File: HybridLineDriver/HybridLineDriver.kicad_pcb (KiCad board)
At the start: 2 copper layers, 100 x 100 mm, 34 parts, among them J1 XLR3, J2 Conn_01x03, J3 Conn_01x02, U1 OPA1679

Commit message: update layout
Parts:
- moved R8 4.05 mm to (99.5, 100.5)
- moved R5 3.25 mm to (102.5, 105.0)
- moved R3 2.50 mm to (104.1, 92.5)
- moved R2 2.24 mm to (104.1, 95.5)
- moved R7 1.12 mm to (88.0, 90.0)
- moved R16 1.00 mm to (85.7, 95.5)
- moved C3 0.93 mm to (90.1, 98.0)
- moved R4 0.62 mm to (91.5, 101.5)
- moved C10 0.27 mm to (96.5, 105.9)
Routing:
- net Net-(C1-Pad2): track 30.2 -> 26.4 mm
- net Net-(U1C-+): track 15.0 -> 11.5 mm
- net Net-(U1C--): track 23.3 -> 21.1 mm
- net Net-(C6-Pad1): track 142.2 -> 140.6 mm
- net Net-(R2-Pad1): track 28.9 -> 27.7 mm
- net Net-(U1B--): track 17.1 -> 16.0 mm
- net Net-(C2-Pad1): track 94.6 -> 93.6 mm
- net Net-(R16-Pad2): track 15.7 -> 16.7 mm
- net Net-(U1D--): track 14.3 -> 13.3 mm
- net Net-(R7-Pad1): track 11.0 -> 11.8 mm
- net Net-(C3-Pad1): track 47.3 -> 46.7 mm
- net Net-(U1A--): track 9.80 -> 10.4 mm

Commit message: update layout
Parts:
- moved RV1 10.1 mm to (84.1, 83.2)
- moved C6 4.95 mm to (78.4, 133.6)
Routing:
- net Net-(C6-Pad1): track 140.6 -> 131.6 mm
- net Net-(C6-Pad2): track 9.82 -> 14.4 mm
- net Net-(R16-Pad2): track 16.7 -> 12.4 mm
- net Net-(R7-Pad1): track 11.8 -> 7.90 mm
- net GND: track 111.5 -> 110.0 mm
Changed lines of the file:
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@@
 	(footprint "Connector_PinHeader_2.54mm:PinHeader_1x03_P2.54mm_Vertical"
 		(layer "F.Cu")
-		(at 74 83 90)
+		(at 84.074 83.185 90)
 		(descr "Through hole straight pin header, 1x03, 2.54mm pitch, single row")
 		(tags "Through hole pin header THT 1x03 2.54mm single row")
@@
 	(footprint "Capacitor_THT:CP_Radial_D8.0mm_P3.50mm"
 		(layer "F.Cu")
-		(at 73.406 133.604 180)
+		(at 78.359 133.604 180)
 		(descr "CP, Radial series, Radial, pin pitch=3.50mm, , diameter=8mm, Electrolytic Capacitor")
 		(tags "CP Radial series Radial pin pitch 3.50mm  diameter 8mm Electrolytic Capacitor")
@@
 	)
 	(segment
-		(start 73.406 109.594)
-		(end 85.598 97.402)
+		(start 89 90)
+		(end 89.4625 90)
 		(width 0.254)
 		(layer "F.Cu")
@@
 	)
 	(segment
-		(start 104 104.9625)
-		(end 103.9625 105)
+		(start 117.799 128.41444)
+		(end 104.22744 141.986)
 		(width 0.254)
 		(layer "F.Cu")
@@
 	)
 	(segment
-		(start 85.598 97.402)
-		(end 85.598 93.402)
+		(start 85.598 93.402)
+		(end 89 90)
 		(width 0.254)
 		(layer "F.Cu")
@@
 	)
 	(segment
-		(start 75.184 141.986)
-		(end 73.406 140.208)
+		(start 104 104.9625)
+		(end 103.9625 105)
 		(width 0.254)
 		(layer "F.Cu")
@@
 	)
 	(segment
-		(start 117.799 124.437879)
-		(end 117.799 128.41444)
+		(start 78.359 104.641)
+		(end 85.598 97.402)
 		(width 0.254)
 		(layer "F.Cu")
@@
 	)
 	(segment
-		(start 117.799 128.41444)
-		(end 104.22744 141.986)
+		(start 85.598 97.402)
+		(end 85.598 93.402)
 		(width 0.254)
 		(layer "F.Cu")
@@
 	)
 	(segment
-		(start 73.406 133.604)
-		(end 73.406 109.594)
-		(width 0.254)
-		(layer "F.Cu")
-		(net 11)
-	)
-	(segment
-		(start 73.406 140.208)
-		(end 73.406 133.604)
+		(start 117.799 124.437879)
+		(end 117.7375 124.437879)
 		(width 0.254)
 		(layer "F.Cu")
@@
 	)
 	(segment
-		(start 117.799 124.437879)
-		(end 117.7375 124.437879)
+		(start 78.359 136.747)
+		(end 83.598 141.986)
 		(width 0.254)
 		(layer "F.Cu")
@@
 	)
 	(segment
-		(start 89 90)
-		(end 89.4625 90)
+		(start 104 91.5)
+		(end 104 104.9625)
 		(width 0.254)
 		(layer "F.Cu")
@@
 	)
 	(segment
-		(start 104.22744 141.986)
-		(end 75.184 141.986)
+		(start 117.799 124.437879)
+		(end 117.799 128.41444)
 		(width 0.254)
 		(layer "F.Cu")
@@
 	)
 	(segment
-		(start 104 91.5)
-		(end 104 104.9625)
+		(start 78.359 133.604)
+		(end 78.359 136.747)
 		(width 0.254)
 		(layer "F.Cu")
@@
 	)
 	(segment
-		(start 85.598 93.402)
-		(end 89 90)
+		(start 83.598 141.986)
+		(end 104.22744 141.986)
 		(width 0.254)
 		(layer "F.Cu")
@@
 	)
 	(segment
-		(start 69.906 133.604)
-		(end 64.516 133.604)
+		(start 78.359 133.604)
+		(end 78.359 104.641)
 		(width 0.254)
 		(layer "F.Cu")
-		(net 12)
+		(net 11)
 	)
 	(segment
@@
 	)
 	(segment
-		(start 69.906 133.604)
-		(end 69.652 133.858)
+		(start 60.706 133.843)
+		(end 60.706 133.604)
 		(width 0.254)
 		(layer "F.Cu")
@@
 	)
 	(segment
-		(start 60.706 133.843)
-		(end 60.706 133.604)
+		(start 74.859 133.604)
+		(end 64.516 133.604)
 		(width 0.254)
 		(layer "F.Cu")
@@
 	)
 	(segment
-		(start 81.04 87.5)
-		(end 76.54 83)
-		(width 0.254)
-		(layer "F.Cu")
-		(net 15)
-	)
-	(segment
 		(start 64.516 130.679)
 		(end 64.516 122.174)
@@
 	)
 	(segment
-		(start 83.5 87.5)
-		(end 81.04 87.5)
-		(width 0.254)
-		(layer "F.Cu")
-		(net 15)
-	)
-	(segment
 		(start 108.799621 143.168379)
 		(end 128.016 123.952)
@@
 	)
 	(segment
+		(start 76.708 140.5235)
+		(end 76.708 133.096)
+		(width 0.254)
+		(layer "F.Cu")
+		(net 15)
+	)
+	(segment
 		(start 97.731379 121.353379)
 		(end 97.79 121.412)
@@
 	)
 	(segment
+		(start 70.612 127)
+		(end 70.612 122.174)
+		(width 0.254)
+		(layer "F.Cu")
+		(net 15)
+	)
+	(segment
 		(start 94.488 103.378)
 		(end 94.488 103.632)
@@
 	)
 	(segment
+		(start 85.725 87.63)
+		(end 86.614 86.741)
+		(width 0.254)
+		(layer "F.Cu")
+		(net 15)
+	)
+	(segment
 		(start 87.827 124.437879)
 		(end 83.842121 124.437879)
@@
 	)
 	(segment
+		(start 86.614 86.741)
+		(end 86.614 83.185)
+		(width 0.254)
+		(layer "F.Cu")
+		(net 15)
+	)
+	(segment
 		(start 112.7145 123.19)
 		(end 114.3 123.19)
@@
 	)
 	(segment
-		(start 99.003 143.168379)
-		(end 108.799621 143.168379)
+		(start 76.708 133.096)
+		(end 70.612 127)
 		(width 0.254)
 		(layer "F.Cu")
@@
 	)
 	(segment
-		(start 96.5 100.5)
-		(end 98.0375 100.5)
+		(start 99.003 143.168379)
+		(end 108.799621 143.168379)
 		(width 0.254)
 		(layer "F.Cu")
@@
 	)
 	(segment
-		(start 76.708 140.5235)
-		(end 76.708 122.174)
+		(start 96.5 100.5)
+		(end 98.0375 100.5)
 		(width 0.254)
 		(layer "F.Cu")
@@
 	)
 	(via
-		(at 83.5 87.5)
+		(at 85.725 87.63)
 		(size 0.8)
 		(drill 0.4)
@@
 	)
 	(via
-		(at 76.708 122.174)
+		(at 70.612 122.174)
 		(size 0.8)
 		(drill 0.4)
@@
 	)
 	(segment
-		(start 79.08 83)
-		(end 82.0375 83)
+		(start 89.154 86.741)
+		(end 86.5375 89.3575)
 		(width 0.254)
 		(layer "F.Cu")
@@
 	)
 	(segment
-		(start 82.0375 83)
-		(end 86.5375 87.5)
+		(start 86.5375 89.3575)
+		(end 86.5375 90)
 		(width 0.254)
 		(layer "F.Cu")
@@
 	)
 	(segment
-		(start 86.5375 87.5)
-		(end 86.5375 90)
+		(start 89.154 83.185)
+		(end 89.154 86.741)
 		(width 0.254)
 		(layer "F.Cu")
@@
 	)
 	(segment
+		(start 84.201 93.193)
+		(end 84.201 83.312)
+		(width 0.254)
+		(layer "F.Cu")
+		(net 21)
+	)
+	(segment
+		(start 84.201 83.312)
+		(end 84.074 83.185)
+		(width 0.254)
+		(layer "F.Cu")
+		(net 21)
+	)
+	(segment
 		(start 84.197 95.5)
 		(end 84.197 93.197)
@@
 	(segment
 		(start 84.197 93.197)
-		(end 74 83)
+		(end 84.201 93.193)
 		(width 0.254)
 		(layer "F.Cu")

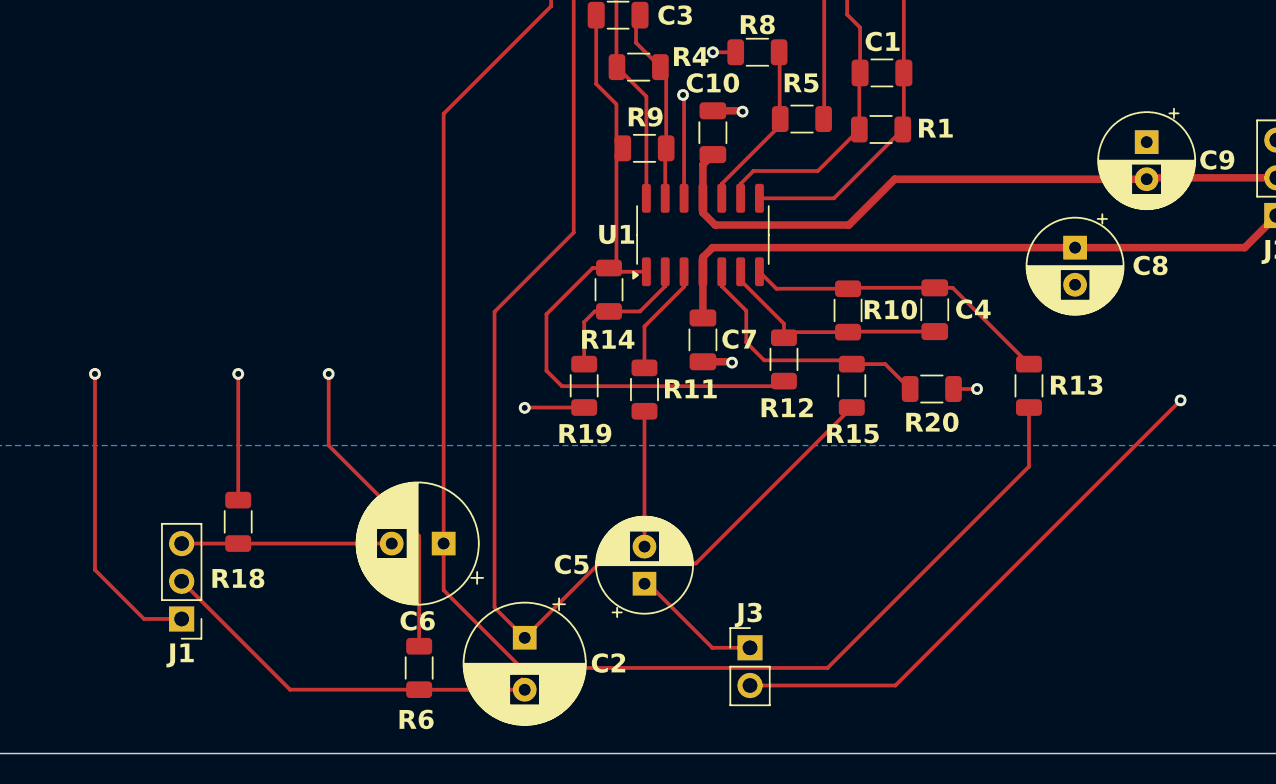
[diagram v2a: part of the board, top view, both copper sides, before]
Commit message: Update HybridLineDriver.kicad_pcb
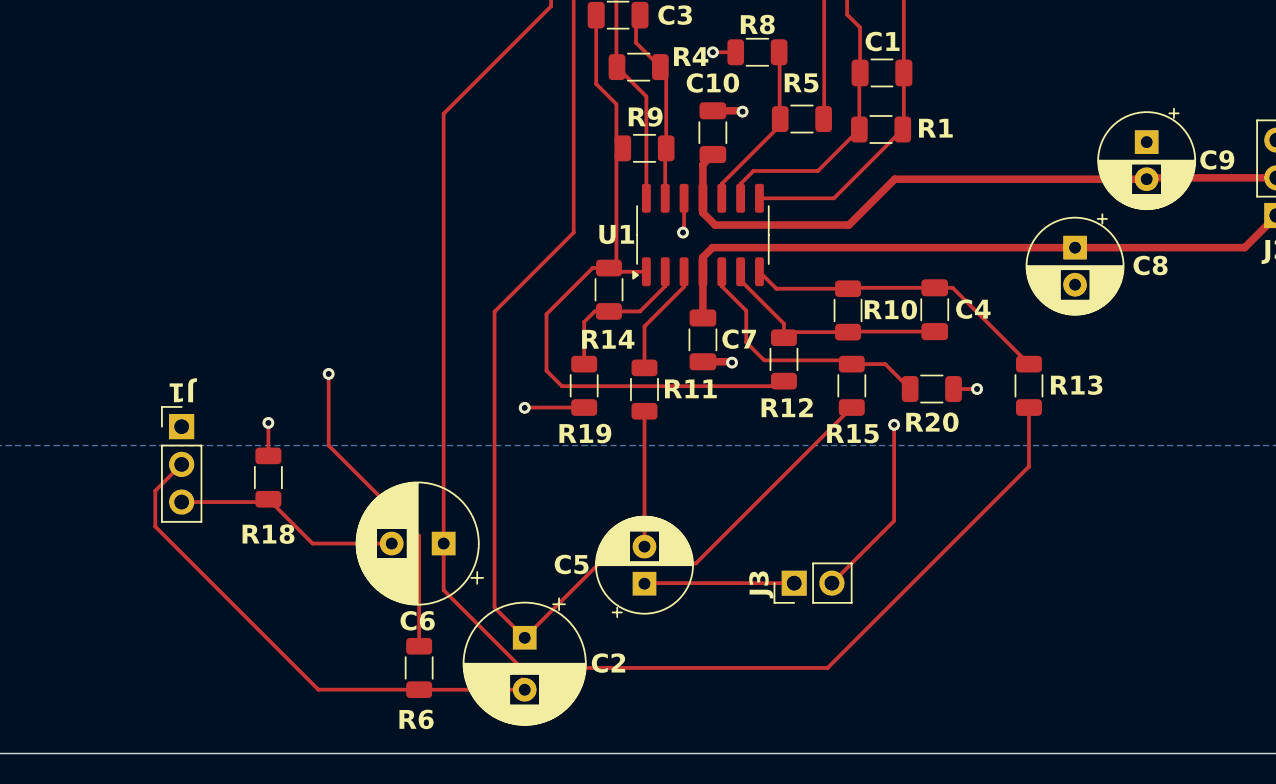
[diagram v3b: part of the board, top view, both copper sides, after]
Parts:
- moved J1 13.0 mm to (60.7, 125.7), turned to 0 degrees
- moved J3 5.28 mm to (102.0, 136.3), turned to 90 degrees
- moved R18 3.61 mm to (66.5, 129.2)
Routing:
- net GND: track 110.0 -> 53.8 mm, vias 11 -> 10
- net Net-(C2-Pad2): track 27.3 -> 35.2 mm
- net Net-(J3-Pin_1): track 8.90 -> 10.1 mm
- net Net-(C6-Pad2): track 14.4 -> 15.5 mm

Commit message: massive pcb rework
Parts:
- moved J1 78.1 mm to (134.5, 100.2), turned to 180 degrees
- moved R18 70.9 mm to (128.5, 94.7), turned to 90 degrees
- moved R6 63.7 mm to (124.8, 100.2)
- moved C6 51.5 mm to (110.4, 93.2), turned to 0 degrees
- moved C2 50.3 mm to (116.2, 101.5), turned to 0 degrees
- moved J3 36.1 mm to (134.2, 120.1), turned to 0 degrees
- moved R13 35.6 mm to (86.2, 106.4), turned to 90 degrees
- moved R20 27.9 mm to (95.1, 100.4), turned to -90 degrees
- moved C3 27.0 mm to (100.7, 122.8)
- moved R15 26.1 mm to (92.8, 100.4), turned to 90 degrees
- moved C5 25.2 mm to (111.9, 120.9), turned to 180 degrees
- moved C4 24.6 mm to (90.6, 104.8), turned to 180 degrees
- moved R10 18.3 mm to (90.6, 107.4), turned to 180 degrees
- moved R4 18.3 mm to (102.0, 116.5), turned to 90 degrees
- moved RV1 17.3 mm to (97.5, 94.1)
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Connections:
- C3 pad 2: Net-(U1D--) -> Net-(U1B--)
- C4 pad 1: Net-(U1B--) -> Net-(U1D--)
- R10 pad 1: Net-(U1B--) -> Net-(U1D--)
- R12 pad 2: Net-(U1B--) -> Net-(U1D--)
- R15 pad 1: Net-(U1B-+) -> Net-(U1D-+)
- R20 pad 2: Net-(U1B-+) -> Net-(U1D-+)
- R4 pad 1: Net-(U1D--) -> Net-(U1B--)
- R9 pad 2: Net-(U1D--) -> Net-(U1B--)
- U1 pad 12: GND -> Net-(U1D-+)
- U1 pad 14: Net-(R2-Pad1) -> Net-(C4-Pad2)
- U1 pad 5: Net-(U1B-+) -> GND
- U1 pad 7: Net-(C4-Pad2) -> Net-(R2-Pad1)
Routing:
- net Net-(C6-Pad1): track 131.6 -> 36.8 mm
- net Net-(C2-Pad1): track 93.6 -> 29.3 mm
- net GND: track 53.8 -> 14.4 mm, vias 10 -> 8
- net Net-(C3-Pad1): track 46.7 -> 26.9 mm
- net Net-(C2-Pad2): track 35.2 -> 16.5 mm
- net Net-(U1B-+): track 17.8 -> 0.00 mm
- net Net-(J3-Pin_1): track 10.1 -> 22.7 mm
- net Net-(U1D-+): track 0.00 -> 11.0 mm
- net Net-(C1-Pad2): track 26.4 -> 15.6 mm
- net Net-(C5-Pad2): track 9.12 -> 19.2 mm
- net Net-(U1C--): track 21.1 -> 12.4 mm
- net Net-(C4-Pad2): track 20.8 -> 12.5 mm
- net Net-(U1B--): track 16.0 -> 9.86 mm
- net Net-(C6-Pad2): track 15.5 -> 21.5 mm
- net Net-(R2-Pad1): track 27.7 -> 22.4 mm
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
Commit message: pcb update
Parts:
- moved R16 0.28 mm to (89.9, 97.4)
- moved R15 0.25 mm to (92.6, 100.4)
- moved R9 0.25 mm to (100.7, 120.3)
- moved C4 0.13 mm to (90.6, 104.6)
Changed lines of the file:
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@@
 	(footprint "Resistor_SMD:R_1206_3216Metric"
 		(layer "F.Cu")
-		(at 100.711 120.523)
+		(at 100.711 120.269)
 		(descr "Resistor SMD 1206 (3216 Metric), square (rectangular) end terminal, IPC_7351 nominal, (Body size source: IPC-SM-782 page 72, https://www.pcb-3d.com/wordpress/wp-content/uploads/ipc-sm-782a_amendment_1_and_2.pdf), generated with kicad-footprint-generator")
 		(tags "resistor")
@@
 		(tags "capacitor")
 		(property "Reference" "C7"
-			(at -0.762 -2.724 0)
+			(at -1.27 -2.47 0)
 			(unlocked yes)
 			(layer "F.SilkS")
@@
 	(footprint "Resistor_SMD:R_1206_3216Metric"
 		(layer "F.Cu")
-		(at 92.837 100.3915 90)
+		(at 92.583 100.3915 90)
 		(descr "Resistor SMD 1206 (3216 Metric), square (rectangular) end terminal, IPC_7351 nominal, (Body size source: IPC-SM-782 page 72, https://www.pcb-3d.com/wordpress/wp-content/uploads/ipc-sm-782a_amendment_1_and_2.pdf), generated with kicad-footprint-generator")
 		(tags "resistor")
@@
 	(footprint "Capacitor_SMD:C_1206_3216Metric"
 		(layer "F.Cu")
-		(at 90.551 104.775 180)
+		(at 90.551 104.648 180)
 		(descr "Capacitor SMD 1206 (3216 Metric), square (rectangular) end terminal, IPC_7351 nominal, (Body size source: IPC-SM-782 page 76, https://www.pcb-3d.com/wordpress/wp-content/uploads/ipc-sm-782a_amendment_1_and_2.pdf), generated with kicad-footprint-generator")
 		(tags "capacitor")
@@
 	(footprint "Resistor_SMD:R_1206_3216Metric"
 		(layer "F.Cu")
-		(at 90.17 97.536 90)
+		(at 89.916 97.409 90)
 		(descr "Resistor SMD 1206 (3216 Metric), square (rectangular) end terminal, IPC_7351 nominal, (Body size source: IPC-SM-782 page 72, https://www.pcb-3d.com/wordpress/wp-content/uploads/ipc-sm-782a_amendment_1_and_2.pdf), generated with kicad-footprint-generator")
 		(tags "resistor")
@@
 	)
 	(gr_rect
-		(start 47.752 47.752)
-		(end 147.752 147.752)
+		(start 42.748 31.788)
+		(end 142.748 131.788)
 		(stroke
 			(width 0.1)
@@
 	)
 	(segment
-		(start 92.026 104.775)
-		(end 92.202 104.951)
+		(start 92.202 104.824)
+		(end 92.202 107.2535)
+		(width 0.254)
+		(layer "F.Cu")
+		(net 1)
+	)
+	(segment
+		(start 92.026 104.648)
+		(end 92.202 104.824)
 		(width 0.254)
 		(layer "F.Cu")
@@
 	)
 	(segment
-		(start 92.202 104.951)
-		(end 92.202 107.2535)
-		(width 0.254)
-		(layer "F.Cu")
-		(net 1)
-	)
-	(segment
 		(start 102.616 110.363)
 		(end 99.660621 110.363)
@@
 	)
 	(segment
-		(start 94.238 100.33)
-		(end 95.631 100.33)
+		(start 92.583 98.929)
+		(end 89.9735 98.929)
 		(width 0.254)
 		(layer "F.Cu")
@@
 	)
 	(segment
-		(start 99.06 103.759)
-		(end 105.4715 103.759)
+		(start 92.583 98.929)
+		(end 93.984 100.33)
 		(width 0.254)
 		(layer "F.Cu")
@@
 	)
 	(segment
-		(start 95.631 100.33)
-		(end 99.06 103.759)
+		(start 99.06 103.759)
+		(end 105.4715 103.759)
 		(width 0.254)
 		(layer "F.Cu")
@@
 	)
 	(segment
-		(start 90.2395 98.929)
-		(end 90.17 98.9985)
+		(start 93.984 100.33)
+		(end 95.631 100.33)
 		(width 0.254)
 		(layer "F.Cu")
@@
 	)
 	(segment
-		(start 115.824 101.092)
-		(end 116.205 101.473)
+		(start 89.9735 98.929)
+		(end 89.916 98.8715)
 		(width 0.254)
 		(layer "F.Cu")
@@
 	)
 	(segment
-		(start 92.837 98.929)
-		(end 90.2395 98.929)
+		(start 115.824 101.092)
+		(end 116.205 101.473)
 		(width 0.254)
 		(layer "F.Cu")
@@
 	)
 	(segment
-		(start 105.4715 103.759)
-		(end 106.6145 102.616)
+		(start 95.631 100.33)
+		(end 99.06 103.759)
 		(width 0.254)
 		(layer "F.Cu")
@@
 	)
 	(segment
-		(start 92.837 98.929)
-		(end 94.238 100.33)
+		(start 108.1385 101.092)
+		(end 115.824 101.092)
 		(width 0.254)
 		(layer "F.Cu")
@@
 	)
 	(segment
-		(start 108.1385 101.092)
-		(end 115.824 101.092)
+		(start 105.4715 103.759)
+		(end 106.6145 102.616)
 		(width 0.254)
 		(layer "F.Cu")
@@
 	)
 	(segment
-		(start 101.981 117.987)
-		(end 100.680885 117.987)
-		(width 0.254)
-		(layer "F.Cu")
-		(net 5)
-	)
-	(segment
 		(start 102.186 122.809)
 		(end 102.1735 122.7965)
@@
 	(segment
 		(start 102.1735 118.5565)
-		(end 102.1735 120.523)
+		(end 102.1735 120.269)
 		(width 0.254)
 		(layer "F.Cu")
@@
 	)
 	(segment
-		(start 101.981 118.364)
-		(end 102.1735 118.5565)
+		(start 102.1735 122.7965)
+		(end 102.1735 120.269)
 		(width 0.254)
 		(layer "F.Cu")
@@
 	)
 	(segment
-		(start 102.1735 122.7965)
-		(end 102.1735 120.523)
+		(start 101.981 117.987)
+		(end 100.680885 117.987)
 		(width 0.254)
 		(layer "F.Cu")
@@
 	)
 	(segment
-		(start 98.368 115.674115)
-		(end 98.368 115.290379)
+		(start 101.981 118.364)
+		(end 102.1735 118.5565)
 		(width 0.254)
 		(layer "F.Cu")
@@
 	)
 	(segment
-		(start 89.414 115.1235)
-		(end 89.5 115.1235)
+		(start 98.368 115.674115)
+		(end 98.368 115.290379)
 		(width 0.254)
 		(layer "F.Cu")
-		(net 6)
+		(net 5)
 	)
 	(segment
-		(start 99.236 122.809)
-		(end 99.2485 122.7965)
+		(start 89.414 115.1235)
+		(end 89.5 115.1235)
 		(width 0.254)
 		(layer "F.Cu")
@@
 	(segment
 		(start 99.2485 122.7965)
-		(end 99.2485 120.523)
+		(end 99.2485 120.269)
 		(width 0.254)
 		(layer "F.Cu")
@@
 	)
 	(segment
+		(start 99.236 122.809)
+		(end 99.2485 122.7965)
+		(width 0.254)
+		(layer "F.Cu")
+		(net 6)
+	)
+	(segment
 		(start 86.614 120.65)
 		(end 86.614 115.1275)
@@
 	)
 	(segment
-		(start 89.076 104.775)
+		(start 89.076 104.648)
 		(end 89.076 107.4545)
 		(width 0.254)
@@
 	(segment
 		(start 89.0885 107.442)
-		(end 89.119621 107.442)
+		(end 89.0885 104.6605)
 		(width 0.254)
 		(layer "F.Cu")
@@
 	)
 	(segment
-		(start 89.076 107.4545)
-		(end 88.642 107.8885)
+		(start 89.0885 107.442)
+		(end 89.119621 107.442)
 		(width 0.254)
 		(layer "F.Cu")
@@
 	)
 	(segment
-		(start 89.0885 107.442)
-		(end 89.0885 104.7875)
+		(start 89.119621 107.442)
+		(end 92.018 110.340379)
 		(width 0.254)
 		(layer "F.Cu")
@@
 	)
 	(segment
-		(start 89.0885 104.7875)
-		(end 89.076 104.775)
+		(start 89.0885 104.6605)
+		(end 89.076 104.648)
 		(width 0.254)
 		(layer "F.Cu")
@@
 	)
 	(segment
-		(start 89.119621 107.442)
-		(end 92.018 110.340379)
+		(start 89.076 107.4545)
+		(end 88.642 107.8885)
 		(width 0.254)
 		(layer "F.Cu")
@@
 	)
 	(segment
-		(start 100.9015 100.457)
-		(end 102.616 100.457)
+		(start 110.363 93.218)
+		(end 110.363 93.98)
 		(width 0.254)
 		(layer "F.Cu")
@@
 	)
 	(segment
-		(start 110.363 93.218)
-		(end 110.363 93.98)
+		(start 86.233 99.695)
+		(end 88.519 97.409)
 		(width 0.254)
 		(layer "F.Cu")
@@
 	)
 	(segment
-		(start 86.233 104.9635)
-		(end 86.233 100.457)
+		(start 97.8535 97.409)
+		(end 100.9015 100.457)
 		(width 0.254)
 		(layer "F.Cu")
@@
 	)
 	(segment
-		(start 86.233 100.457)
-		(end 89.281 97.409)
+		(start 100.9015 100.457)
+		(end 102.616 100.457)
 		(width 0.254)
 		(layer "F.Cu")
@@
 	)
 	(segment
-		(start 110.363 93.98)
-		(end 103.886 100.457)
+		(start 88.519 97.409)
+		(end 97.8535 97.409)
 		(width 0.254)
 		(layer "F.Cu")
@@
 	)
 	(segment
-		(start 89.281 97.409)
-		(end 97.8535 97.409)
+		(start 110.363 93.98)
+		(end 103.886 100.457)
 		(width 0.254)
 		(layer "F.Cu")
@@
 	)
 	(segment
-		(start 97.8535 97.409)
-		(end 100.9015 100.457)
+		(start 86.233 104.9635)
+		(end 86.233 99.695)
 		(width 0.254)
 		(layer "F.Cu")
@@
 	)
 	(segment
-		(start 98.044 117.221)
-		(end 97.098 116.275)
+		(start 98.171 117.094)
+		(end 97.098 116.021)
 		(width 0.254)
 		(layer "F.Cu")
@@
 	)
 	(segment
-		(start 98.171 104.394)
-		(end 96.549 104.394)
-		(width 0.508)
+		(start 97.098 116.021)
+		(end 97.098 115.290379)
+		(width 0.254)
 		(layer "F.Cu")
 		(net 15)
 	)
 	(segment
-		(start 97.098 116.275)
-		(end 97.098 115.290379)
-		(width 0.254)
+		(start 98.171 104.394)
+		(end 96.549 104.394)
+		(width 0.508)
 		(layer "F.Cu")
 		(net 15)
@@
 	)
 	(via
-		(at 98.044 117.221)
+		(at 98.171 117.094)
 		(size 0.8)
 		(drill 0.4)
@@
 	)
 	(segment
-		(start 90.17 96.0735)
-		(end 95.5695 96.0735)
+		(start 89.916 95.9465)
+		(end 90.043 96.0735)
 		(width 0.254)
 		(layer "F.Cu")
@@
 	)
 	(segment
-		(start 92.837 101.854)
-		(end 95.123 101.854)
+		(start 90.043 96.0735)
+		(end 95.5695 96.0735)
 		(width 0.254)
 		(layer "F.Cu")
-		(net 22)
+		(net 21)
 	)
 	(segment
@@
 		(net 22)
 	)
+	(segment
+		(start 92.583 101.854)
+		(end 95.123 101.854)
+		(width 0.254)
+		(layer "F.Cu")
+		(net 22)
+	)
 	(zone
 		(net 0)
@@
 		(polygon
 			(pts
-				(xy 147.701 147.574) (xy 47.879 147.574) (xy 47.658113 79.540453) (xy 147.480113 79.540453)
+				(xy 141.986 131.318) (xy 44.323 130.556) (xy 44.978496 33.949406) (xy 141.097 34.163)
 			)
 		)
